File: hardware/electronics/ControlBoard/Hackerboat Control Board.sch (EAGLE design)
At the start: 235 parts, among them IC1 74AHC1G08DBV, IC2 TINY861L-20SU, IC3 74AHC1G04DBV, J8 AVR_SPI_PRG_6PTH, U1 IPS6041G, U10 INA169, U11 IPS6041G, U12 INA169, U14 TPS54331, U15 TPS54331, U18 ADC128D818, U19 ADC128D818, U2 IPS6041G, U20 IPS6041G, U21 INA169, U22 IPS6041G, U23 INA169, U24 IPS6041G, U25 INA169, U27 INA169, U29 TPS61175, U3 INA169, U4 IPS6041G, U5 INA169, U6 IPS6041G, U7 INA169, U8 IPS6041G, U9 INA169

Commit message: Changed the R/C input over to SBUS. Updates to the PowerDistributionBaord
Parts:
- removed C41, C42: 100n, resistor:C-EUC0603
- removed J8: AVR_SPI_PRG_6PTH, SparkFun-Connectors:AVR_SPI_PRG_6PTH
- removed RC-IN-0, RC-IN-1, RC-IN-2, RC-IN-3, RC-IN-4, RC-IN-5, RC-IN-6, RC-IN-7: (no value), pinhead-1:PINHD-1X3_2.54
- removed U28: (no value), adafruit:TXB0108PWR
- added SBUS-IN, SBUS-OUT: HEADER_POS3_70545, con-molex-c-grid-sl:HEADER_POS3_70545
- added SJ1: (no value), jumper:SJ2W
- C40: value 100n -> (none)
- IC2: value TINY861L-20SU -> 74AUC1G06DBV; device atmel:TINY861L-20SU -> 74xx-little-us:74AUC1G06DBV
- R57: value 10K -> (none)
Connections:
- net AUX_GPIO_3_5V renamed BBB_SCLK_5V
- net AUX_GPIO_4_5V renamed BBB_MOSI_5V
- net AUX_GPIO_5_5V renamed BBB_MISO_5V
- removed net AUX_GPIO_3_3V3: U$1.GPIO2_22, U$4.11, U17.A3
- removed net AUX_GPIO_4_3V3: U$1.GPIO2_23, U$4.10, U17.A6
- removed net AUX_GPIO_5_3V3: U$1.UART4_RTSN, U$4.8, U17.A5
- removed net N$59: IC2.(ADC0/DI/SDA)PA0, U28.A1
- removed net N$60: RC-IN-7.1, U28.B8
- removed net N$61: RC-IN-6.1, U28.B7
- removed net N$64: RC-IN-5.1, U28.B6
- removed net N$65: RC-IN-4.1, U28.B5
- removed net N$66: RC-IN-3.1, U28.B4
- removed net N$67: RC-IN-2.1, U28.B3
- removed net N$71: RC-IN-1.1, U28.B2
- removed net N$74: RC-IN-0.1, U28.B1
- removed net RC_MODE_SELECT: IC2.(ADC9/INT0/T0)PB6, R57.1, U$1.UART4_CTSN, U$4.7
- removed net RC_RESET: IC2.(ADC10/!RESET!)PB7, J8.5, U$1.GPIO2_12, U$4.5
- net +3V3: now also R57.2; no longer C40.1, C41.1, IC2.AVCC, IC2.VCC, J8.2, U28.OE, U28.VCCA
- net +5V: now also C40.1, IC2G$2.VCC, SBUS-IN.2, SBUS-OUT.2; no longer C42.1, U28.VCCB
- net BBB_MISO: now also U17.A5; no longer IC2.(MISO/DO/OC1A)PB1, J8.1
- net BBB_MOSI: now also U17.A6; no longer IC2.(MOSI/DI/SDA/!OC1A!)PB0, J8.4
- net BBB_SCLK: now also U17.A3; no longer IC2.(SCK/SCL/!OC1B!)PB2, J8.3
- net CELL_TX: now also SJ1.3
- net GND: now also IC2G$2.GND, SBUS-IN.1, SBUS-OUT.1; no longer C41.2, C42.2, IC2.AGND, IC2.GND, J8.6, R57.2, RC-IN-0.3, RC-IN-1.3, RC-IN-2.3, RC-IN-3.3, RC-IN-4.3, RC-IN-5.3, RC-IN-6.3, RC-IN-7.3, U28.GND
- net GNSS_TX: now also SJ1.1
- net N$46: now also U$1.GPIO2_22, U$4.11; no longer IC2.(ADC6/AIN1)PA7, U28.A8
- net N$47: now also U$1.GPIO2_23, U$4.10; no longer IC2.(ADC5/AIN0)PA6, U28.A7
- net N$53: now also IC2G$1.I, SBUS-IN.3, SBUS-OUT.3; no longer IC2.(ADC4/AIN2)PA5, U28.A6
- net N$55: now also IC2G$1.O, R57.1, SJ1.2; no longer IC2.(ADC3/ICP0)PA4, U28.A5
- net N$56: now also U$1.UART4_RTSN, U$4.8; no longer IC2.(AREF)PA3, U28.A4
- net N$57: now also U$1.UART4_CTSN, U$4.7; no longer IC2.(ADC2/INT1/USCK/SCL)PA2, U28.A3
- net N$58: now also U$1.GPIO2_12, U$4.5; no longer IC2.(ADC1/DO)PA1, U28.A2
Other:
- moved on the sheet: C40, R57

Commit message: Making sure we have the latest board in github
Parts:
- removed POWER_MONITOR: (no value), pinhead-1:PINHD-2X6_2.54
- added D21, D22, D23, D24, D25, D26, D27, D28: 5V, adafruit:DIODESOD-123
- added DISARM: AMB, adafruit:LEDCHIPLED_0805
- added ENABLE, RLY0, RLY1, RLY2, RLY3, RLY4, RLY5: GRN, adafruit:LEDCHIPLED_0805
- added HORN-RLY: RED, adafruit:LEDCHIPLED_0805
- added POWER_MON: (no value), pinhead-1:PINHD-2X6_2.54
- added R62, R63, R64, R65, R66, R67, R68, R87, R88, R89, R90, R91, R92, R93, R94, R95, R96: 1K, resistor:R-EU_R0603
- 5V-STAT, 7V4-STAT, PWR: value (none) -> GRN
- C40: value (none) -> 100n
- H1, H3, H4, H7, SJ1, U$1: BOM (none) -> EXCLUDE
- R49: value (none) -> 110K
- R50: value (none) -> 15K
- R57: value (none) -> 10K
- REV: value (none) -> RED
- renumbered S1 to CELL
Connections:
- removed net BBB_UART0_DTR: BBB_CONSOLE.1, J3.1, SERIAL_CONSOLE.1
- new net N$59: R62.1, RLY0.A
- new net N$60: R63.1, RLY1.A
- new net N$61: R64.1, RLY2.A
- new net N$64: DISARM.A, R68.1
- new net N$65: R65.1, RLY3.A
- new net N$66: R66.1, RLY4.A
- new net N$67: R67.1, RLY5.A
- new net N$71: ENABLE.A, R87.1
- new net N$74: HORN-RLY.A, R88.1
- new net N$87: J4.1, POWER_STATE.1, R89.1
- new net N$88: J4.2, POWER_STATE.2, R90.1
- new net N$89: J1.2, R92.1, STEERING.2
- new net N$90: J3.2, R93.1, SERIAL_CONSOLE.2
- new net N$91: J3.3, R94.1, SERIAL_CONSOLE.3
- new net N$92: J2.2, R95.1, STATUS_LIGHTS.2
- new net N$93: BBB_RESET.2, J10.2, R96.1
- new net SBUS_IN_5V: R91.1, SBUS-IN.3, SBUS-OUT.3
- net +5V: now also POWER_MON.1, POWER_MON.5, POWER_MON.9; no longer POWER_MONITOR.1, POWER_MONITOR.5, POWER_MONITOR.9
- net AUX_ADC_0: now also POWER_MON.10; no longer POWER_MONITOR.10
- net AUX_ADC_1: now also POWER_MON.11; no longer POWER_MONITOR.11
- net BBB_STATUS_LIGHTS_5V: now also D27.C, R95.2; no longer J2.2, STATUS_LIGHTS.2
- net BBB_UART0_RX: now also D26.C, R93.2; no longer J3.2, SERIAL_CONSOLE.2
- net BBB_UART0_TX: now also D25.C, R94.2; no longer J3.3, SERIAL_CONSOLE.3
- net CHARGE_CURRENT: now also POWER_MON.7; no longer POWER_MONITOR.7
- net CHARGE_VOLTAGE: now also POWER_MON.6; no longer POWER_MONITOR.6
- net DISARM_RELAY_IN_5V: now also D22.C, R90.2; no longer J4.2, POWER_STATE.2
- net ENABLE_RELAY_IN_5V: now also D23.C, R89.2; no longer J4.1, POWER_STATE.1
- net GND: now also D21.A, D22.A, D23.A, D24.A, D25.A, D26.A, D27.A, D28.A, DISARM.C, ENABLE.C, HORN-RLY.C, POWER_MON.12, POWER_MON.4, POWER_MON.8, RLY0.C, RLY1.C, RLY2.C, RLY3.C, RLY4.C, RLY5.C; no longer POWER_MONITOR.12, POWER_MONITOR.4, POWER_MONITOR.8
- net MOT_CURRENT: now also POWER_MON.3; no longer POWER_MONITOR.3
- net MOT_VOLTAGE: now also POWER_MON.2; no longer POWER_MONITOR.2
- net N$23: now also D28.C, R96.2; no longer BBB_RESET.2, J10.2
- net N$53: now also D21.C, R91.2; no longer SBUS-IN.3, SBUS-OUT.3
- net RELAY_OUT_0: now also R62.2
- net RELAY_OUT_1: now also R63.2
- net RELAY_OUT_2: now also R64.2
- net RELAY_OUT_3: now also R65.2
- net RELAY_OUT_4: now also R66.2
- net RELAY_OUT_5: now also R67.2
- net RELAY_OUT_DISARM: now also R68.2
- net RELAY_OUT_ENABLE: now also R87.2
- net RELAY_OUT_HORN: now also R88.2
- net SERVO_RUDDER_5V: now also D24.C, R92.2; no longer J1.2, STEERING.2
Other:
- note added: "AUXILIARY DIGITAL I/O"
- note added: "MOTOR CONTROL RELAY OUTPUT"
- note added: "POWER STATUS"

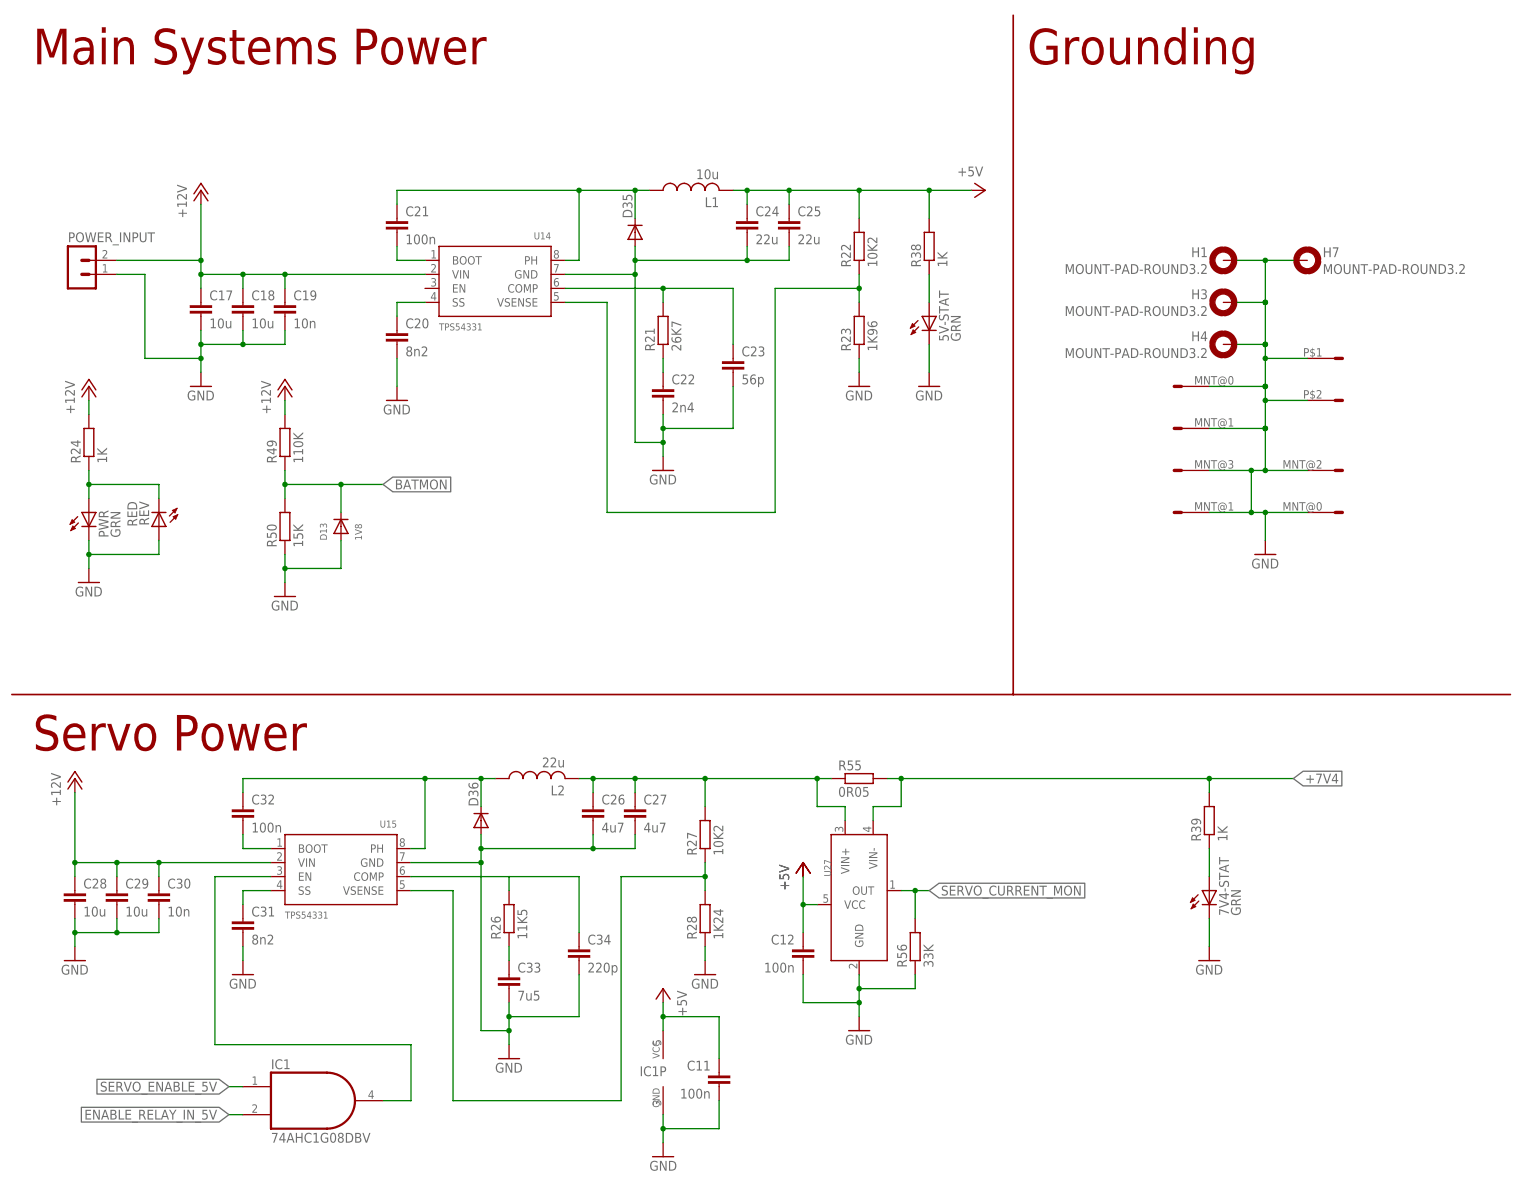
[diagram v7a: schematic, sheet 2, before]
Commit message: Added mode and dataflow diagrams. Updated board schematic and layout with comments from hardware review.
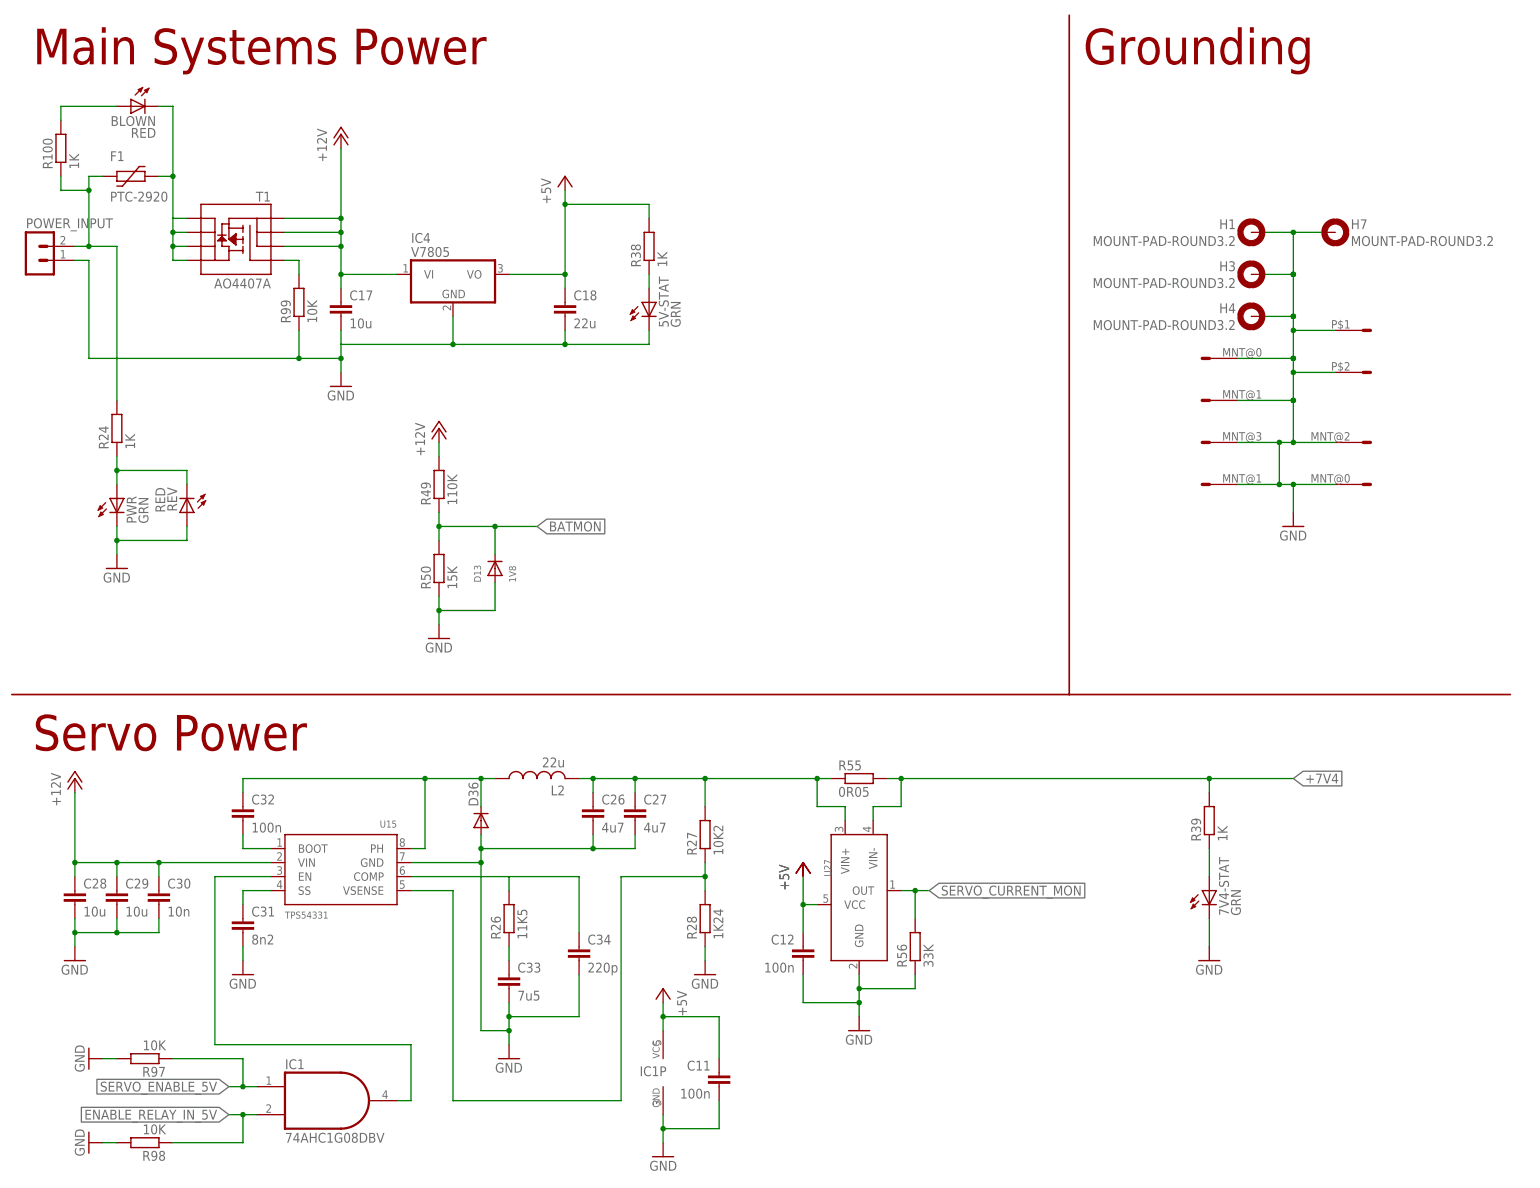
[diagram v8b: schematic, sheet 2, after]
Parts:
- removed C21: 100n, resistor:C-EUC0603
- removed C22: 2n4, resistor:C-EUC0603
- removed C23: 56p, resistor:C-EUC0603
- removed C24, C25: 22u, resistor:C-EUC1210
- removed D35: (no value), ARD-SRG-MOT8-1a:SPARKFUN_DIODESMA
- removed L1: 10u, logos-inductors:NR6045
- removed R21: 26K7, resistor:R-EU_R0603
- removed R22: 10K2, resistor:R-EU_R0603
- removed R23: 1K96, resistor:R-EU_R0603
- removed U14: TPS54331, logos-power:TPS54331
- added 15V-ENB, SJ2: (no value), jumper:SJ
- added BLOWN, FAULT_0, FAULT_1, FAULT_2, FAULT_3, FAULT_4, FAULT_5, FAULT_DISARM, FAULT_ENABLE, FAULT_HORN: RED, adafruit:LEDCHIPLED_0805
- added C41, C42, C49, C50: 1000p, res-cap-arrays:4CAP0805
- added F1, F2: PTC-2920, fuses:PTC-2920
- added IC4: V7805, linear:7805TV
- added IC5: 7805TV, linear:7805TV
- added R100, R101, R102, R103, R104, R105, R106, R107, R108, R109: 1K, resistor:R-EU_R0603
- added R110, R111, R112, R113: (no value), res-cap-arrays:4R-NCTS742C083
- added R97, R98, R99: 10K, resistor:R-EU_R0603
- added T1: AO4407A, SparkFun-DiscreteSemi:MOSFET-PCHANNEL-SOIC8SOIC8
- C18: value 10u -> 22u
- C19: value 10n -> 10u; device resistor:C-EUC0603 -> resistor:C-EUC1210
- C20: value 8n2 -> 22u; device resistor:C-EUC0603 -> resistor:C-EUC1210
- R51, R52, R53, R54: value 4u7 -> 4K7
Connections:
- removed net N$63: C21.1, D35.C, L1.1, U14.PH
- removed net N$69: C20.1, U14.SS
- removed net N$70: C23.1, R21.2, U14.COMP
- removed net N$73: R22.1, R23.2, U14.VSENSE
- new net N$100: FAULT_0.A, R101.1
- new net N$101: FAULT_1.A, R102.1
- new net N$102: FAULT_2.A, R103.1
- new net N$103: FAULT_3.A, R104.1
- new net N$105: FAULT_4.A, R105.1
- new net N$109: FAULT_5.A, R106.1
- new net N$110: FAULT_ENABLE.A, R107.1
- new net N$111: FAULT_DISARM.A, R108.1
- new net N$112: FAULT_HORN.A, R109.1
- new net N$113: C41D.1, R110A.1, U18.IN0
- new net N$114: C41C.1, R110B.1, U18.IN1
- new net N$115: C49D.1, R112A.1, U19.IN0
- new net N$116: C41B.1, R110C.1, U18.IN2
- new net N$118: C41A.1, R110D.1, U18.IN3
- new net N$122: C42D.1, R111A.1, U18.IN4
- new net N$123: C42C.1, R111B.1, U18.IN5
- new net N$124: C42B.1, R111C.1, U18.IN6
- new net N$125: C42A.1, R111D.1, U18.IN7
- new net N$126: C49C.1, R112B.1, U19.IN1
- new net N$127: C49B.1, R112C.1, U19.IN2
- new net N$128: C49A.1, R112D.1, U19.IN3
- new net N$129: C50D.1, R113A.1, U19.IN4
- new net N$130: C50C.1, R113B.1, U19.IN5
- new net N$131: C50B.1, R113C.1, U19.IN6
- new net N$132: C50A.1, R113D.1, U19.IN7
- new net N$94: 15V-ENB.2, L3.1, U29.EN, U29.VIN
- new net N$95: J4.5, POWER_STATE.5, SJ2.1
- new net N$96: BLOWN.C, F1.2, T1.D@1, T1.D@2, T1.D@3, T1.D@4
- new net N$97: R99.2, T1.G
- new net N$98: F1.1, POWER_INPUT.2, R100.1, R24.2
- new net N$99: BLOWN.A, R100.2
- net +12V: now also 15V-ENB.1, IC4.VI, IC5.VI, T1.S@1, T1.S@2, T1.S@3; no longer C18.1, L3.1, POWER_INPUT.2, R24.2, U14.VIN, U29.EN, U29.VIN
- net +5V: now also C18.1, IC4.VO, R101.2, R102.2, R103.2, R104.2, R105.2, R106.2, R107.2, R108.2, R109.2; no longer C24.1, C25.1, J2.1, L1.2, R22.2, STATUS_LIGHTS.1
- net AUX_ADC_0: now also R113B.2; no longer U19.IN5
- net AUX_ADC_1: now also R113C.2; no longer U19.IN6
- net CHARGE_CURRENT: now also R113A.2; no longer U19.IN4
- net CHARGE_VOLTAGE: now also R112D.2; no longer U19.IN3
- net ENABLE_RELAY_IN_5V: now also R98.1
- net GND: now also C41A.2, C41B.2, C41C.2, C41D.2, C42A.2, C42B.2, C42C.2, C42D.2, C49A.2, C49B.2, C49C.2, C49D.2, C50A.2, C50B.2, C50C.2, C50D.2, IC4.GND, IC5.GND, R97.2, R98.2, R99.1; no longer C22.2, C23.2, C24.2, C25.2, D35.A, R23.1, U14.GND
- net MOT_CURRENT: now also R112B.2; no longer U19.IN1
- net MOT_VOLTAGE: now also R112C.2; no longer U19.IN2
- net N$62: now also F2.1, J2.1, STATUS_LIGHTS.1; no longer C21.2, U14.BOOT
- net N$68: now also C20.1, F2.2, IC5.VO; no longer C22.1, R21.1
- net RELAY_CURRENT_0: now also R110A.2; no longer U18.IN0
- net RELAY_CURRENT_1: now also R110B.2; no longer U18.IN1
- net RELAY_CURRENT_2: now also R110C.2; no longer U18.IN2
- net RELAY_CURRENT_3: now also R110D.2; no longer U18.IN3
- net RELAY_CURRENT_4: now also R111A.2; no longer U18.IN4
- net RELAY_CURRENT_5: now also R111B.2; no longer U18.IN5
- net RELAY_CURRENT_DISARM: now also R111C.2; no longer U18.IN6
- net RELAY_CURRENT_ENABLE: now also R111D.2; no longer U18.IN7
- net RELAY_CURRENT_HORN: now also R112A.2; no longer U19.IN0
- net RELAY_DISARM_FAULT: now also FAULT_DISARM.C
- net RELAY_ENABLE_FAULT: now also FAULT_ENABLE.C
- net RELAY_FAULT_0: now also FAULT_0.C
- net RELAY_FAULT_1: now also FAULT_1.C
- net RELAY_FAULT_2: now also FAULT_2.C
- net RELAY_FAULT_3: now also FAULT_3.C
- net RELAY_FAULT_4: now also FAULT_4.C
- net RELAY_FAULT_5: now also FAULT_5.C
- net RELAY_HORN_FAULT: now also FAULT_HORN.C
- net RELAY_OUT_ENABLE: now also SJ2.2; no longer J4.5, POWER_STATE.5
- net SERVO_CURRENT_MON: now also R113D.2; no longer U19.IN7
- net SERVO_ENABLE_5V: now also R97.1
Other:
- note added: "FAULT LIGHTS"
- moved on the sheet: 5V-STAT, ACC_POWER, C10, C17, C18, C47, D13, H1, H3, H4, H7, IC1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
